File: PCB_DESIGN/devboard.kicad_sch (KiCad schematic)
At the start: 30 parts, among them J1 USB_C_Receptacle_USB2.0_14P, SW1 SW_Push, U1 RP2040, U2 NCP1117-3.3_SOT223, U3 W25Q128JVS, Y1 12 MHz

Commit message: forgot to save schematic
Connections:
- net GPIO0: no longer U1.17 (GPIO14), U1.27 (GPIO16), U1.29 (GPIO18), U1.31 (GPIO20), U1.34 (GPIO22), U1.36 (GPIO24), U1.38 (GPIO26_ADC0), U1.40 (GPIO28_ADC2)
- net GPIO1: no longer U1.16 (GPIO13), U1.18 (GPIO15), U1.28 (GPIO17), U1.30 (GPIO19), U1.32 (GPIO21), U1.35 (GPIO23), U1.37 (GPIO25), U1.39 (GPIO27_ADC1), U1.41 (GPIO29_ADC3)
- new net GPIO13: U1.16 (GPIO13)
- new net GPIO14: U1.17 (GPIO14)
- new net GPIO15: U1.18 (GPIO15)
- new net GPIO16: U1.27 (GPIO16)
- new net GPIO17: U1.28 (GPIO17)
- new net GPIO18: U1.29 (GPIO18)
- new net GPIO19: U1.30 (GPIO19)
- new net GPIO20: U1.31 (GPIO20)
- new net GPIO21: U1.32 (GPIO21)
- new net GPIO22: U1.34 (GPIO22)
- new net GPIO23: U1.35 (GPIO23)
- new net GPIO24: U1.36 (GPIO24)
- new net GPIO25: U1.37 (GPIO25)
- new net GPIO26_ADC0: U1.38 (GPIO26_ADC0)
- new net GPIO27_ADC1: U1.39 (GPIO27_ADC1)
- new net GPIO28_ADC2: U1.40 (GPIO28_ADC2)
- new net GPIO29_ADC3: U1.41 (GPIO29_ADC3)
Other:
- moved on the sheet: R3, R4, U1

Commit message: almost done pin headers
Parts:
- added J2, J3: Conn_02x18_Odd_Even, symbol Connector_Generic:Conn_02x18_Odd_Even
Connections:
- net +3V3: now also J2.2 (Pin_2)
- net GND: now also J2.1 (Pin_1), J2.11 (Pin_11), J2.13 (Pin_13), J2.15 (Pin_15), J2.17 (Pin_17), J2.19 (Pin_19), J2.21 (Pin_21), J2.23 (Pin_23), J2.25 (Pin_25), J2.27 (Pin_27), J2.29 (Pin_29), J2.3 (Pin_3), J2.31 (Pin_31), J2.33 (Pin_33), J2.35 (Pin_35), J2.36 (Pin_36), J2.5 (Pin_5), J2.7 (Pin_7), J2.9 (Pin_9), J3.10 (Pin_10), J3.12 (Pin_12), J3.14 (Pin_14), J3.16 (Pin_16), J3.18 (Pin_18), J3.2 (Pin_2), J3.20 (Pin_20), J3.22 (Pin_22), J3.24 (Pin_24), J3.26 (Pin_26), J3.28 (Pin_28), J3.30 (Pin_30), J3.32 (Pin_32), J3.34 (Pin_34), J3.35 (Pin_35), J3.36 (Pin_36), J3.4 (Pin_4), J3.6 (Pin_6), J3.8 (Pin_8)
- net GPIO0: now also J2.4 (Pin_4)
- net GPIO1: now also J2.6 (Pin_6)
- net GPIO10: now also J2.24 (Pin_24)
- net GPIO11: now also J2.26 (Pin_26)
- net GPIO12: now also J2.28 (Pin_28)
- net GPIO13: now also J2.30 (Pin_30)
- net GPIO14: now also J2.32 (Pin_32)
- net GPIO15: now also J2.34 (Pin_34)
- net GPIO2: now also J2.8 (Pin_8)
- net GPIO3: now also J2.10 (Pin_10)
- net GPIO4: now also J2.12 (Pin_12)
- net GPIO5: now also J2.14 (Pin_14)
- net GPIO6: now also J2.16 (Pin_16)
- net GPIO7: now also J2.18 (Pin_18)
- net GPIO8: now also J2.20 (Pin_20)
- net GPIO9: now also J2.22 (Pin_22)
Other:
- moved on the sheet: C1, C10, C11, C12, C15, C16, C17, C2, C3, C4, C5, C6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

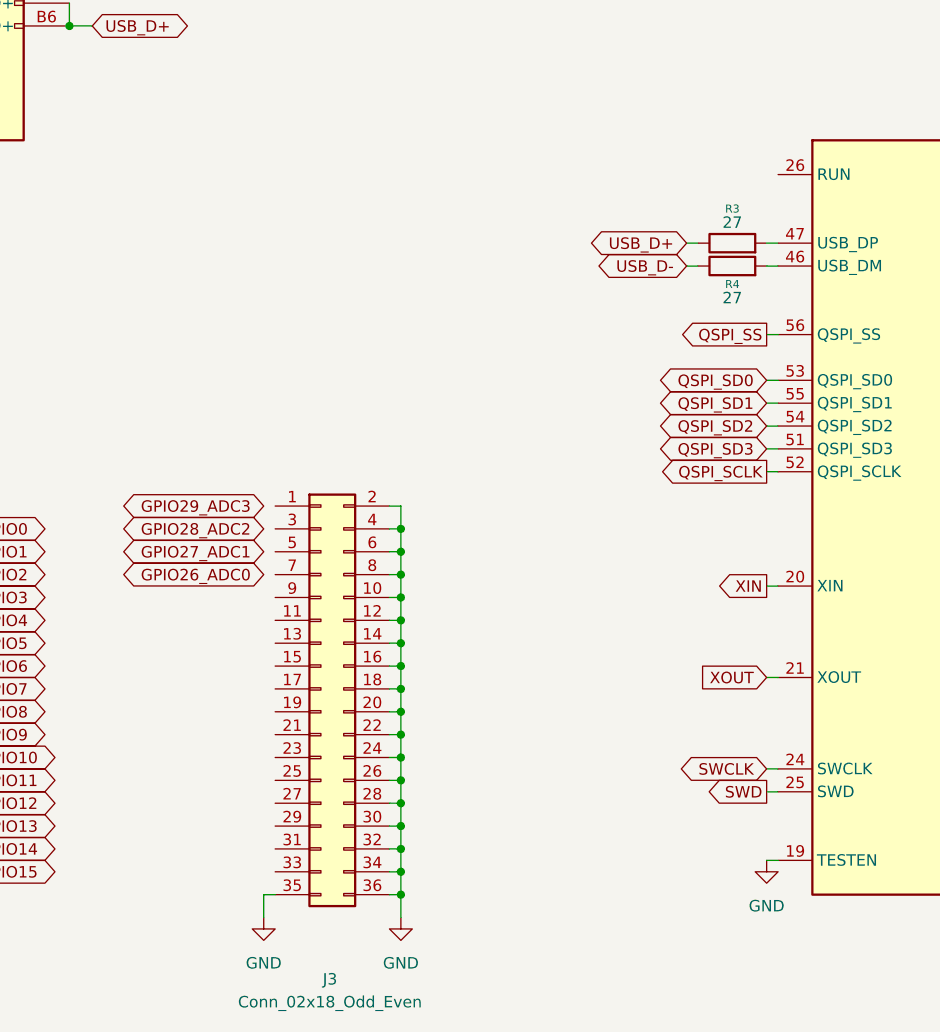
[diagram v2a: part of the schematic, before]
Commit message: finished adding in the I/O headers
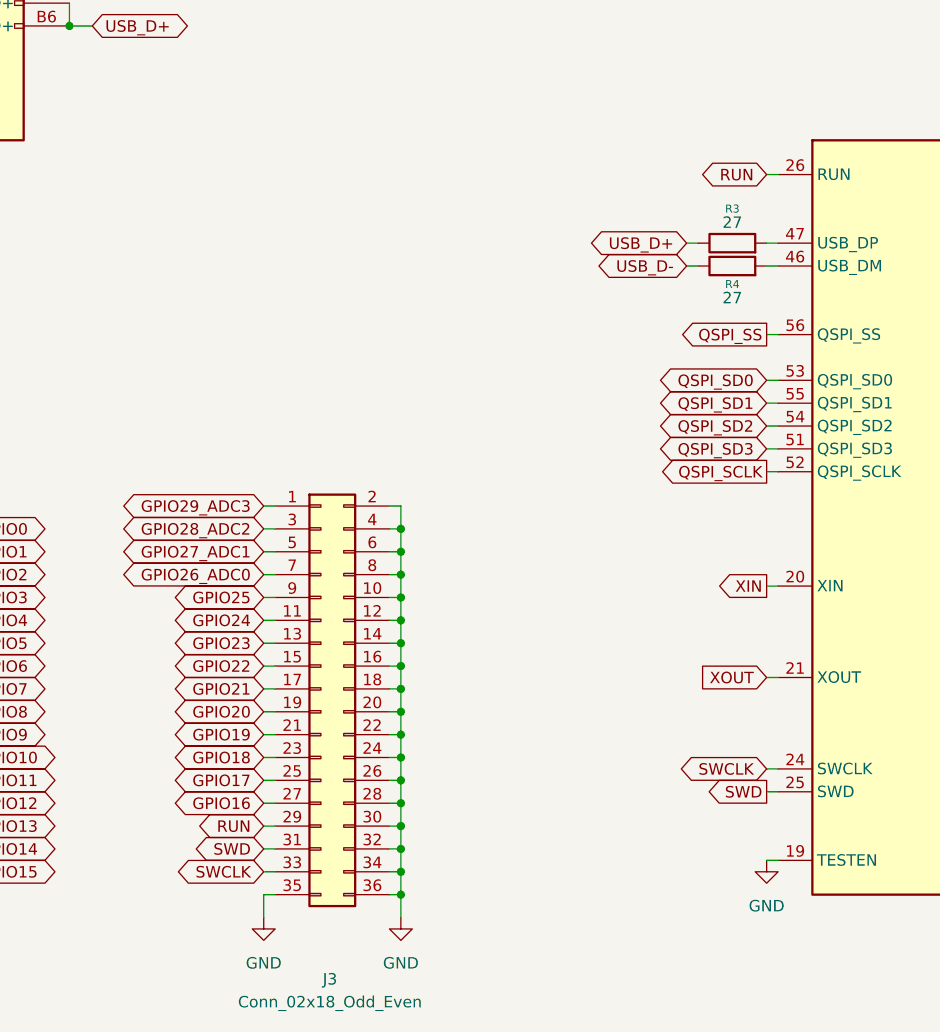
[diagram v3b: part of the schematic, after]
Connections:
- net GPIO16: now also J3.27 (Pin_27)
- net GPIO17: now also J3.25 (Pin_25)
- net GPIO18: now also J3.23 (Pin_23)
- net GPIO19: now also J3.21 (Pin_21)
- net GPIO20: now also J3.19 (Pin_19)
- net GPIO21: now also J3.17 (Pin_17)
- net GPIO22: now also J3.15 (Pin_15)
- net GPIO23: now also J3.13 (Pin_13)
- net GPIO24: now also J3.11 (Pin_11)
- net GPIO25: now also J3.9 (Pin_9)
- net GPIO26_ADC0: now also J3.7 (Pin_7)
- net GPIO27_ADC1: now also J3.5 (Pin_5)
- net GPIO28_ADC2: now also J3.3 (Pin_3)
- net GPIO29_ADC3: now also J3.1 (Pin_1)
- net SWCLK: now also J3.33 (Pin_33)
- net SWD: now also J3.31 (Pin_31)
- net RUN: now reaches J3.29 (Pin_29)
- net RUN: now also U1.26 (RUN)

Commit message: organizing schematic
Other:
- note added: "Crystal Oscillator"
- note added: "Flash Memory/Storage"
- note added: "I/O Headers"
- note added: "USB-C/Power"
- moved on the sheet: C1, C10, C11, C12, C13, C14, C15, C16, C17, C2, C3, C4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

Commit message: working on footprints and journalled organizaton
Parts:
- C1, C10, C11, C12, C15, C16, C17, C2, C3, C4, C5, C6, C7, C8, C9: footprint (none) -> Capacitor_SMD:C_0402_1005Metric
- C13, C14: footprint (none) -> Capacitor_SMD:C_0603_1608Metric
- R1, R2, R3, R4, R5, R6, R7: footprint (none) -> Resistor_SMD:R_0402_1005Metric
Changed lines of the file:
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@@
 			)
 		)
-		(property "Footprint" ""
+		(property "Footprint" "Capacitor_SMD:C_0402_1005Metric"
 			(at 236.22 100.6348 0)
 			(effects
@@
 			)
 		)
-		(property "Footprint" ""
+		(property "Footprint" "Capacitor_SMD:C_0402_1005Metric"
 			(at 130.5052 35.56 0)
 			(effects
@@
 			)
 		)
-		(property "Footprint" ""
+		(property "Footprint" "Resistor_SMD:R_0402_1005Metric"
 			(at 240.538 45.72 90)
 			(effects
@@
 			)
 		)
-		(property "Footprint" ""
+		(property "Footprint" "Capacitor_SMD:C_0402_1005Metric"
 			(at 150.8252 35.56 0)
 			(effects
@@
 			)
 		)
-		(property "Footprint" ""
+		(property "Footprint" "Capacitor_SMD:C_0402_1005Metric"
 			(at 267.97 38.4048 0)
 			(effects
@@
 			)
 		)
-		(property "Footprint" ""
+		(property "Footprint" "Resistor_SMD:R_0402_1005Metric"
 			(at 133.35 72.898 90)
 			(effects
@@
 			)
 		)
-		(property "Footprint" ""
+		(property "Footprint" "Capacitor_SMD:C_0402_1005Metric"
 			(at 195.2752 35.56 0)
 			(effects
@@
 			)
 		)
-		(property "Footprint" ""
+		(property "Footprint" "Capacitor_SMD:C_0402_1005Metric"
 			(at 136.8552 35.56 0)
 			(effects
@@
 			)
 		)
-		(property "Footprint" ""
+		(property "Footprint" "Resistor_SMD:R_0402_1005Metric"
 			(at 133.35 75.438 90)
 			(effects
@@
 			)
 		)
-		(property "Footprint" ""
+		(property "Footprint" "Capacitor_SMD:C_0402_1005Metric"
 			(at 176.2252 35.56 0)
 			(effects
@@
 			)
 		)
-		(property "Footprint" ""
+		(property "Footprint" "Capacitor_SMD:C_0402_1005Metric"
 			(at 188.9252 35.56 0)
 			(effects
@@
 			)
 		)
-		(property "Footprint" ""
+		(property "Footprint" "Capacitor_SMD:C_0402_1005Metric"
 			(at 124.1552 35.56 0)
 			(effects
@@
 			)
 		)
-		(property "Footprint" ""
+		(property "Footprint" "Capacitor_SMD:C_0402_1005Metric"
 			(at 201.6252 35.56 0)
 			(effects
@@
 			)
 		)
-		(property "Footprint" ""
+		(property "Footprint" "Capacitor_SMD:C_0402_1005Metric"
 			(at 163.5252 35.56 0)
 			(effects
@@
 			)
 		)
-		(property "Footprint" ""
+		(property "Footprint" "Resistor_SMD:R_0402_1005Metric"
 			(at 229.87 49.022 90)
 			(effects
@@
 			)
 		)
-		(property "Footprint" ""
+		(property "Footprint" "Capacitor_SMD:C_0402_1005Metric"
 			(at 157.1752 35.56 0)
 			(effects
@@
 			)
 		)
-		(property "Footprint" ""
+		(property "Footprint" "Capacitor_SMD:C_0402_1005Metric"
 			(at 169.8752 35.56 0)
 			(effects
@@
 			)
 		)
-		(property "Footprint" ""
+		(property "Footprint" "Capacitor_SMD:C_0402_1005Metric"
 			(at 182.5752 35.56 0)
 			(effects
@@
 			)
 		)
-		(property "Footprint" ""
+		(property "Footprint" "Resistor_SMD:R_0402_1005Metric"
 			(at 55.88 39.878 90)
 			(effects
@@
 			)
 		)
-		(property "Footprint" ""
+		(property "Footprint" "Resistor_SMD:R_0402_1005Metric"
 			(at 55.88 42.418 90)
 			(effects
@@
 			)
 		)
-		(property "Footprint" ""
+		(property "Footprint" "Capacitor_SMD:C_0603_1608Metric"
 			(at 73.3552 40.64 0)
 			(effects
@@
 			)
 		)
-		(property "Footprint" ""
+		(property "Footprint" "Resistor_SMD:R_0402_1005Metric"
 			(at 257.81 113.538 90)
 			(effects
@@
 			)
 		)
-		(property "Footprint" ""
+		(property "Footprint" "Capacitor_SMD:C_0402_1005Metric"
 			(at 236.22 110.7948 0)
 			(effects
@@
 			)
 		)
-		(property "Footprint" ""
+		(property "Footprint" "Capacitor_SMD:C_0603_1608Metric"
 			(at 96.2152 40.64 0)
 			(effects

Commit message: update the footprint journal
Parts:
- C15, C16: value 15pF -> 33pF
- J1: footprint (none) -> Connector_USB:USB_C_Receptacle_HRO_TYPE-C-31-M-12
- J2, J3: footprint (none) -> Connector_PinHeader_2.54mm:PinHeader_2x18_P2.54mm_Vertical
- SW1: footprint (none) -> Button_Switch_SMD:SW_Push_SPST_NO_Alps_SKRK
- Y1: footprint (none) -> Crystal:Crystal_SMD_3225-4Pin_3.2x2.5mm
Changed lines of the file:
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@@
 			)
 		)
-		(property "Value" "15pF"
+		(property "Value" "33pF"
 			(at 232.41 98.044 90)
 			(effects
@@
 			)
 		)
-		(property "Footprint" ""
+		(property "Footprint" "Connector_PinHeader_2.54mm:PinHeader_2x18_P2.54mm_Vertical"
 			(at 35.56 119.38 0)
 			(effects
@@
 			)
 		)
-		(property "Footprint" ""
+		(property "Footprint" "Crystal:Crystal_SMD_3225-4Pin_3.2x2.5mm"
 			(at 245.11 106.68 0)
 			(effects
@@
 			)
 		)
-		(property "Footprint" ""
+		(property "Footprint" "Connector_PinHeader_2.54mm:PinHeader_2x18_P2.54mm_Vertical"
 			(at 83.82 119.38 0)
 			(effects
@@
 			)
 		)
-		(property "Footprint" ""
+		(property "Footprint" "Connector_USB:USB_C_Receptacle_HRO_TYPE-C-31-M-12"
 			(at 39.37 48.26 0)
 			(effects
@@
 			)
 		)
-		(property "Footprint" ""
+		(property "Footprint" "Button_Switch_SMD:SW_Push_SPST_NO_Alps_SKRK"
 			(at 219.71 45.72 0)
 			(effects
@@
 			)
 		)
-		(property "Value" "15pF"
+		(property "Value" "33pF"
 			(at 232.41 108.204 90)
 			(effects

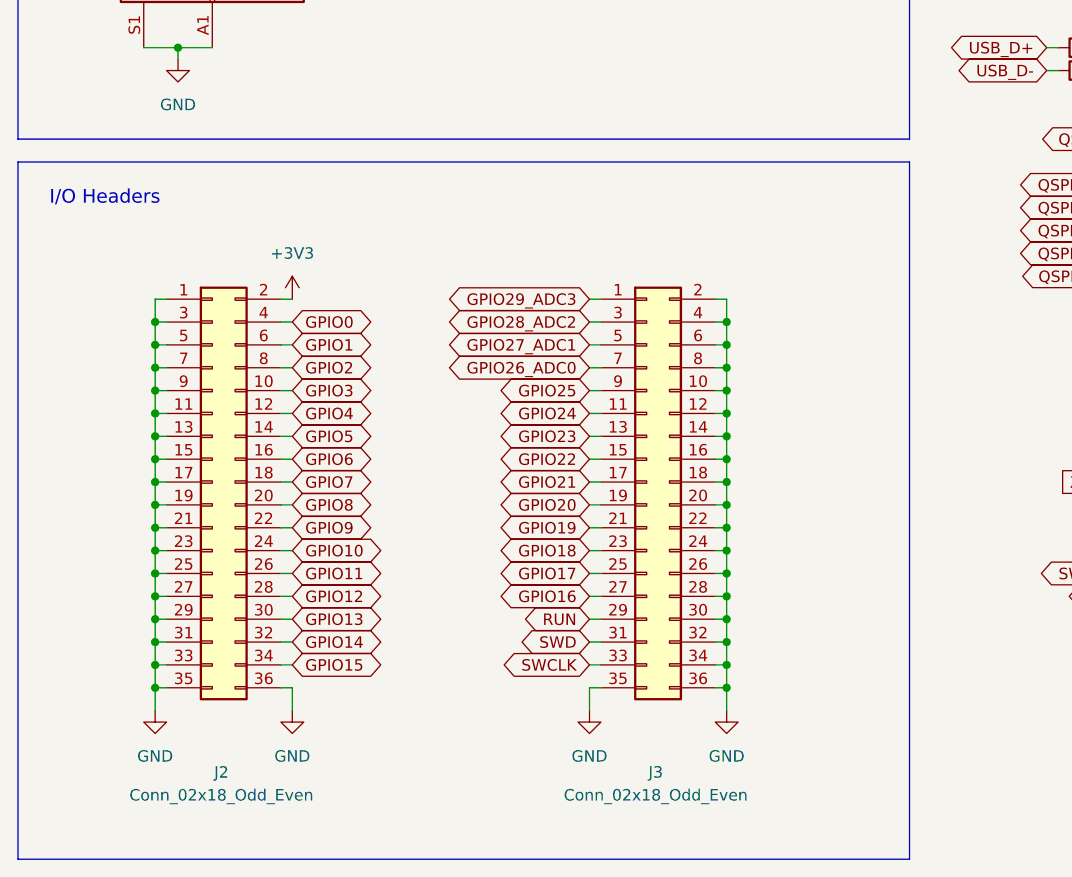
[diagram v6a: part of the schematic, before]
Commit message: working on changing headers to be correct
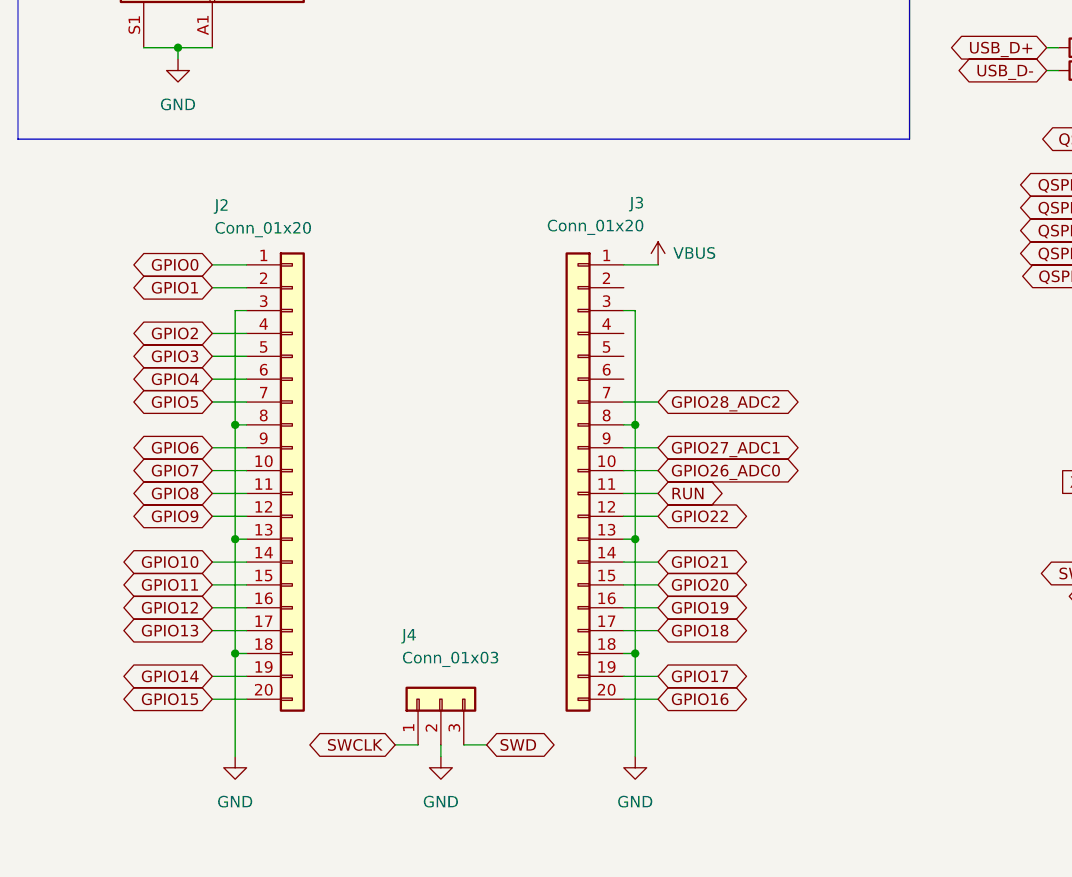
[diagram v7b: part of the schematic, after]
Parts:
- removed J2, J3: Conn_02x18_Odd_Even, Connector_PinHeader_2.54mm:PinHeader_2x18_P2.54mm_Vertical, symbol Connector_Generic:Conn_02x18_Odd_Even
- added J2, J3: Conn_01x20, symbol Connector_Generic:Conn_01x20
- added J4: Conn_01x03, symbol Connector_Generic:Conn_01x03
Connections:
- net GND: now also J2.13 (Pin_13), J2.18 (Pin_18), J2.3 (Pin_3), J2.8 (Pin_8), J3.13 (Pin_13), J3.18 (Pin_18), J3.3 (Pin_3), J3.8 (Pin_8), J4.2 (Pin_2)
- net GPIO0: now also J2.1 (Pin_1)
- net GPIO1: now also J2.2 (Pin_2)
- net GPIO10: now also J2.14 (Pin_14)
- net GPIO11: now also J2.15 (Pin_15)
- net GPIO12: now also J2.16 (Pin_16)
- net GPIO13: now also J2.17 (Pin_17)
- net GPIO14: now also J2.19 (Pin_19)
- net GPIO15: now also J2.20 (Pin_20)
- net GPIO16: now also J3.20 (Pin_20)
- net GPIO17: now also J3.19 (Pin_19)
- net GPIO18: now also J3.17 (Pin_17)
- net GPIO19: now also J3.16 (Pin_16)
- net GPIO2: now also J2.4 (Pin_4)
- net GPIO20: now also J3.15 (Pin_15)
- net GPIO21: now also J3.14 (Pin_14)
- net GPIO22: now also J3.12 (Pin_12)
- net GPIO26_ADC0: now also J3.10 (Pin_10)
- net GPIO27_ADC1: now also J3.9 (Pin_9)
- net GPIO28_ADC2: now also J3.7 (Pin_7)
- net GPIO3: now also J2.5 (Pin_5)
- net GPIO4: now also J2.6 (Pin_6)
- net GPIO5: now also J2.7 (Pin_7)
- net GPIO6: now also J2.9 (Pin_9)
- net GPIO7: now also J2.10 (Pin_10)
- net GPIO8: now also J2.11 (Pin_11)
- net GPIO9: now also J2.12 (Pin_12)
- net RUN: now also J3.11 (Pin_11)
- net SWCLK: now also J4.1 (Pin_1)
- net SWD: now also J4.3 (Pin_3)
- net VBUS: now also J3.1 (Pin_1)
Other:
- note removed: "I/O Headers"

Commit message: finishing the schematic refined
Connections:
- net +3V3: now also J3.5 (Pin_5)
- net GPIO23: now also J3.10 (Pin_10)
- net GPIO24: now also J3.9 (Pin_9)
- net GPIO26_ADC0: now also J3.7 (Pin_7); no longer J3.10 (Pin_10)
- net GPIO27_ADC1: now also J3.6 (Pin_6); no longer J3.9 (Pin_9)
- net GPIO28_ADC2: now also J3.4 (Pin_4); no longer J3.7 (Pin_7)
- net GPIO29_ADC3: now also J3.2 (Pin_2)
- net GPIO25: no longer names the net of U1.37 (GPIO25)
- no-connect marks 0 -> 1
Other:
- moved on the sheet: J2, J3, J4
